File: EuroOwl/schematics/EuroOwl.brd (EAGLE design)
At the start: 100 x 99.8 mm, 121 parts, among them IC1 QUAD_OPAMPD, IC2 QUAD_OPAMPD, Q900 BC846, Q901 BC846, X1 USBPTH-VERTICAL

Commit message: Revision 01
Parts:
- R902: value 100R\ -> 100R
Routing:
- net PA2: track 64.4 -> 63.7 mm
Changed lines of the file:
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@@
 </element>
 <element name="C300" library="resistor" package="C0603" value="100n" x="71.12" y="50.8" smashed="yes">
-<attribute name="NAME" x="72.136" y="50.2285" size="1.016" layer="25" ratio="10"/>
+<attribute name="NAME" x="68.326" y="51.816" size="1.016" layer="25" ratio="10"/>
 <attribute name="VALUE" x="67.691" y="48.006" size="1.27" layer="27" ratio="10"/>
 </element>
@@
 </element>
 <element name="C500" library="resistor" package="C0603" value="100n" x="10.16" y="53.34" smashed="yes">
-<attribute name="NAME" x="9.271" y="54.102" size="1.016" layer="25"/>
+<attribute name="NAME" x="8.636" y="54.102" size="1.016" layer="25"/>
 <attribute name="VALUE" x="9.271" y="51.308" size="1.27" layer="27"/>
 </element>
@@
 <attribute name="NAME" x="73.0885" y="7.112" size="1.016" layer="25"/>
 </element>
-<element name="R902" library="Rebel" package="0603" value="100R\" x="74.93" y="11.43" smashed="yes">
+<element name="R902" library="Rebel" package="0603" value="100R" x="74.93" y="11.43" smashed="yes">
 <attribute name="NAME" x="73.0885" y="12.192" size="1.016" layer="25"/>
 </element>
@@
 </element>
 <element name="Q901" library="transistor" package="SOT23" value="BC846" x="17.78" y="21.59" smashed="yes" rot="R180">
-<attribute name="NAME" x="16.1925" y="23.1775" size="1.016" layer="25"/>
+<attribute name="NAME" x="16.1925" y="23.495" size="1.016" layer="25"/>
 <attribute name="VALUE" x="19.685" y="24.765" size="1.27" layer="27" rot="R180"/>
 </element>
 <element name="D300" library="diode" package="SOT23" value="BAT54S" x="71.12" y="54.61" smashed="yes" rot="R180">
-<attribute name="NAME" x="69.5325" y="56.1975" size="1.016" layer="25"/>
+<attribute name="NAME" x="69.5325" y="56.515" size="1.016" layer="25"/>
 <attribute name="VALUE" x="73.025" y="57.785" size="1.27" layer="27" rot="R180"/>
 </element>
 <element name="Q900" library="transistor" package="SOT23" value="BC846" x="80.01" y="7.62" smashed="yes">
-<attribute name="NAME" x="78.105" y="9.2075" size="1.016" layer="25"/>
+<attribute name="NAME" x="78.105" y="9.525" size="1.016" layer="25"/>
 <attribute name="VALUE" x="78.105" y="4.445" size="1.27" layer="27"/>
 </element>
@@
 </element>
 <element name="D500" library="diode" package="SOT23" value="BAT54S" x="6.35" y="56.1975" smashed="yes" rot="R180">
-<attribute name="NAME" x="4.7625" y="57.785" size="1.016" layer="25"/>
+<attribute name="NAME" x="4.7625" y="58.1025" size="1.016" layer="25"/>
 <attribute name="VALUE" x="8.255" y="59.3725" size="1.27" layer="27" rot="R180"/>
 </element>
 <element name="D600" library="diode" package="SOT23" value="BAT54S" x="6.35" y="35.56" smashed="yes">
-<attribute name="NAME" x="8.255" y="33.9725" size="1.016" layer="25" rot="R180"/>
+<attribute name="NAME" x="4.7625" y="37.465" size="1.016" layer="25"/>
 <attribute name="VALUE" x="4.445" y="32.385" size="1.27" layer="27"/>
 </element>
 <element name="D700" library="diode" package="SOT23" value="BAT54S" x="13.97" y="35.56" smashed="yes">
-<attribute name="NAME" x="15.875" y="33.9725" size="1.016" layer="25" font="vector" rot="R180"/>
+<attribute name="NAME" x="12.3825" y="37.465" size="1.016" layer="25" font="vector"/>
 <attribute name="VALUE" x="12.065" y="32.385" size="1.27" layer="27"/>
 </element>
 <element name="D800" library="diode" package="SOT23" value="BAT54S" x="13.97" y="55.88" smashed="yes" rot="R180">
-<attribute name="NAME" x="12.3825" y="57.4675" size="1.016" layer="25"/>
+<attribute name="NAME" x="14.605" y="57.785" size="1.016" layer="25"/>
 <attribute name="VALUE" x="15.875" y="59.055" size="1.27" layer="27" rot="R180"/>
 </element>
@@
 </element>
 <element name="C501" library="resistor" package="C0603" value="100n" x="71.12" y="40.64" smashed="yes">
-<attribute name="NAME" x="68.0085" y="38.862" size="1.016" layer="25"/>
+<attribute name="NAME" x="68.326" y="38.862" size="1.016" layer="25"/>
 <attribute name="VALUE" x="70.231" y="38.608" size="1.27" layer="27"/>
 </element>
@@
 <wire x1="54.61" y1="5.08" x2="60.325" y2="5.08" width="0.4064" layer="1"/>
 <wire x1="60.325" y1="5.08" x2="62.865" y2="7.62" width="0.4064" layer="1"/>
-<wire x1="62.865" y1="7.62" x2="66.04" y2="7.62" width="0.4064" layer="1"/>
-<via x="66.04" y="7.62" extent="1-16" drill="0.6"/>
-<wire x1="66.04" y1="7.62" x2="66.04" y2="10.16" width="0.4064" layer="16"/>
-<wire x1="66.04" y1="10.16" x2="67.31" y2="11.43" width="0.4064" layer="16"/>
+<wire x1="62.865" y1="7.62" x2="64.77" y2="7.62" width="0.4064" layer="1"/>
+<via x="64.77" y="7.62" extent="1-16" drill="0.6"/>
+<wire x1="64.77" y1="7.62" x2="64.77" y2="8.89" width="0.4064" layer="16"/>
+<wire x1="64.77" y1="8.89" x2="67.31" y2="11.43" width="0.4064" layer="16"/>
 <wire x1="67.31" y1="11.43" x2="67.31" y2="18.415" width="0.4064" layer="16"/>
 <wire x1="67.31" y1="18.415" x2="67.945" y2="19.05" width="0.4064" layer="16"/>

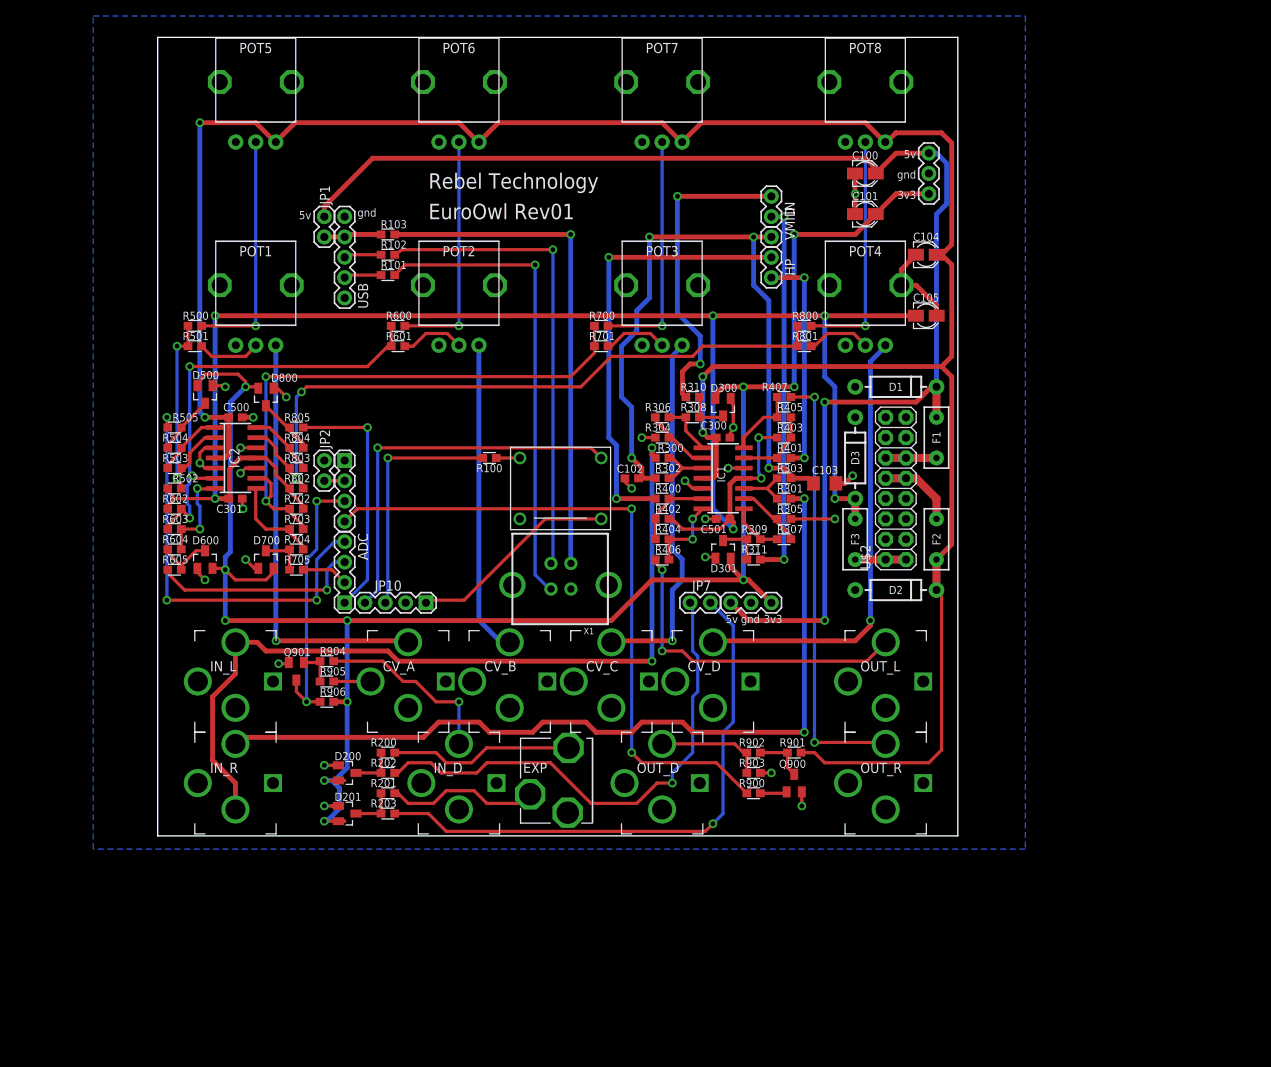
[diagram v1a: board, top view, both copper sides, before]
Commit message: changed input circuit to double inverting op amps
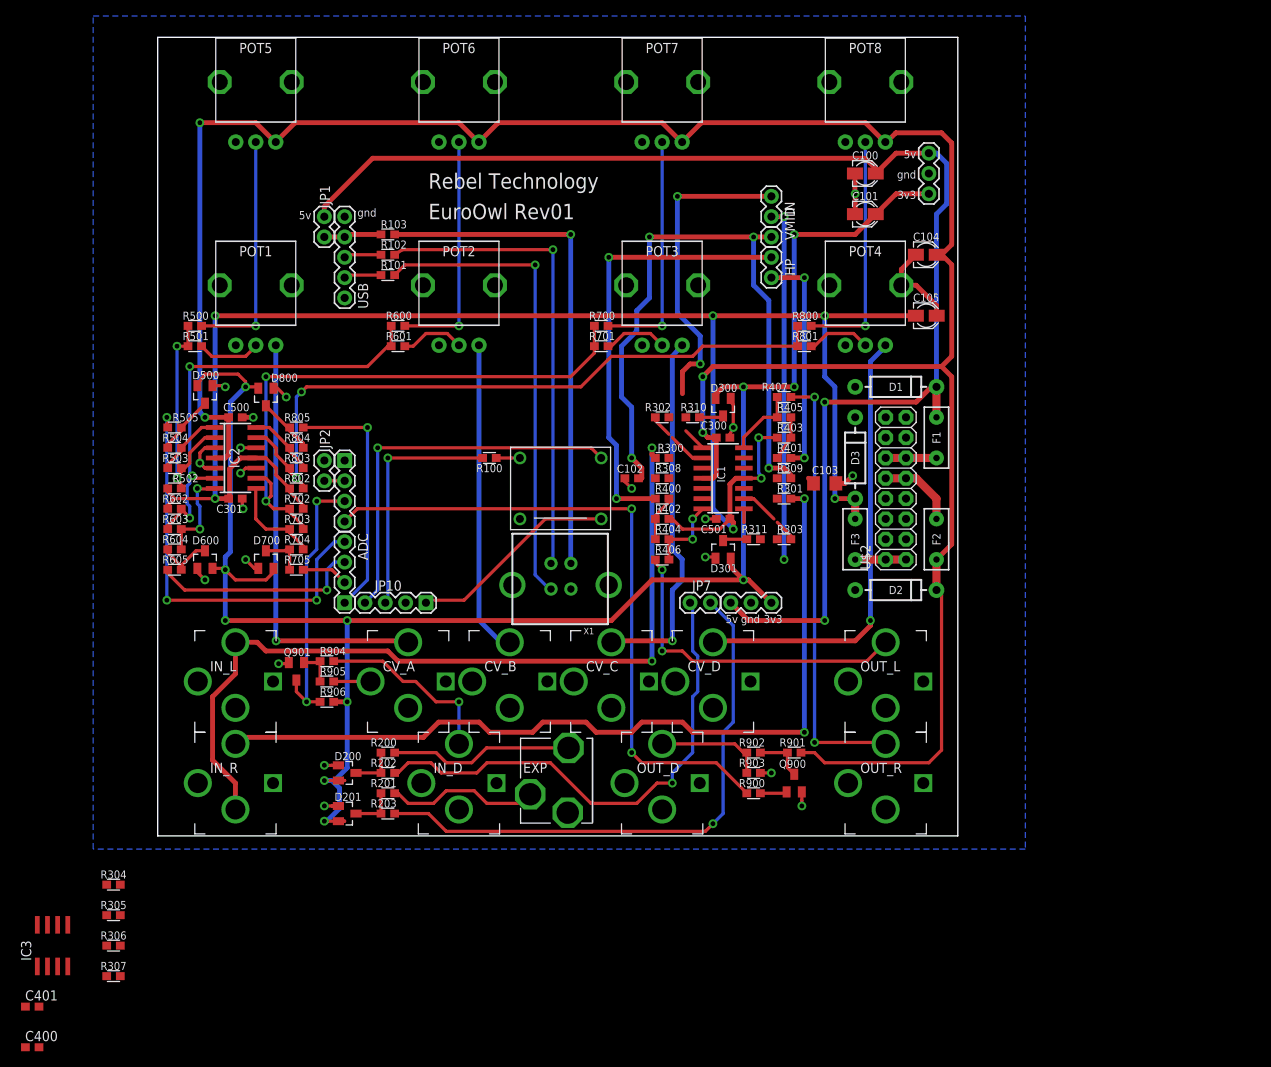
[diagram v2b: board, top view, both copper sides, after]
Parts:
- added C400, C401: 100n, resistor:C0603
- added IC3: TL072D, linear:SO08
- R302, R303: value 33k -> 100k
- R306, R307: value 33k -> 220k
- R308, R309: value 100R -> 33k
- R310, R311: value 100R -> 1k
- moved R307 100.0 mm to (-5.08, -16.5)
- moved R305 97.4 mm to (-5.08, -8.89)
- moved R306 95.2 mm to (-5.08, -12.7), turned to 0 degrees
- moved R304 88.5 mm to (-5.08, -5.08)
- moved R308 8.52 mm to (63.5, 45.7)
- moved R309 8.52 mm to (78.7, 45.7)
- moved R302 7.62 mm to (63.5, 53.3)
- moved R303 7.62 mm to (78.7, 38.1)
- moved R310 2.54 mm to (67.3, 53.3), turned to 180 degrees
- moved R311 2.54 mm to (74.9, 38.1), turned to 0 degrees
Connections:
- removed net N$11: IC1.3, R300.1, R302.1
- removed net N$8: D301.3, R309.1, R311.2
- new net N$53: IC1.14, R309.1, R311.2
- new net N$55: IC1.7, R308.1, R310.2
- new net N$57: IC1.3
- net +12V: now also C400.1, IC3.8
- net -12V: now also C401.2, IC3.4, R306.2, R307.2
- net GND: now also C400.2, C401.1, IC1.10, IC3.3, IC3.5; no longer R304.1, R305.2
- net L_IN: now also D300.3
- net N$1: now also R302.1, R304.2; no longer R306.1, R308.2
- net N$32: now also IC1.6, R304.1, R306.1, R308.2; no longer IC1.10, R301.1, R303.1
- net N$39: now also IC3.1; no longer IC1.7
- net N$4: now also R303.1, R305.2; no longer R307.1, R309.2
- net N$40: now also IC3.7; no longer IC1.14
- net N$41: now also IC3.2; no longer IC1.6
- net N$42: now also IC3.6; no longer IC1.13
- net N$5: now also R301.1, R303.2; no longer R305.1, R307.2
- net N$7: now also IC1.13, R305.1, R307.1, R309.2; no longer D300.3, R308.1, R310.2
- net N$9: now also R300.1, R302.2; no longer R304.2, R306.2
- net R_IN: now also D301.3
- net VCC/2: no longer R302.2, R303.2
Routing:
- net GND: track 73.2 -> 61.5 mm, vias 24 -> 20
- net N$11: track 6.91 -> 0.00 mm
- net N$32: track 6.49 -> 0.00 mm
- net N$7: track 5.57 -> 0.00 mm
- net N$8: track 5.57 -> 0.00 mm
- net N$4: track 6.77 -> 1.75 mm
- net VCC/2: track 86.3 -> 82.0 mm
- net N$42: track 9.77 -> 5.60 mm
- net N$41: track 9.95 -> 5.78 mm
- net N$1: track 6.77 -> 2.97 mm
- net L_IN: track 39.9 -> 42.3 mm
- net N$5: track 8.47 -> 7.63 mm
- net N$9: track 8.47 -> 7.63 mm

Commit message: rerouted input around op amp
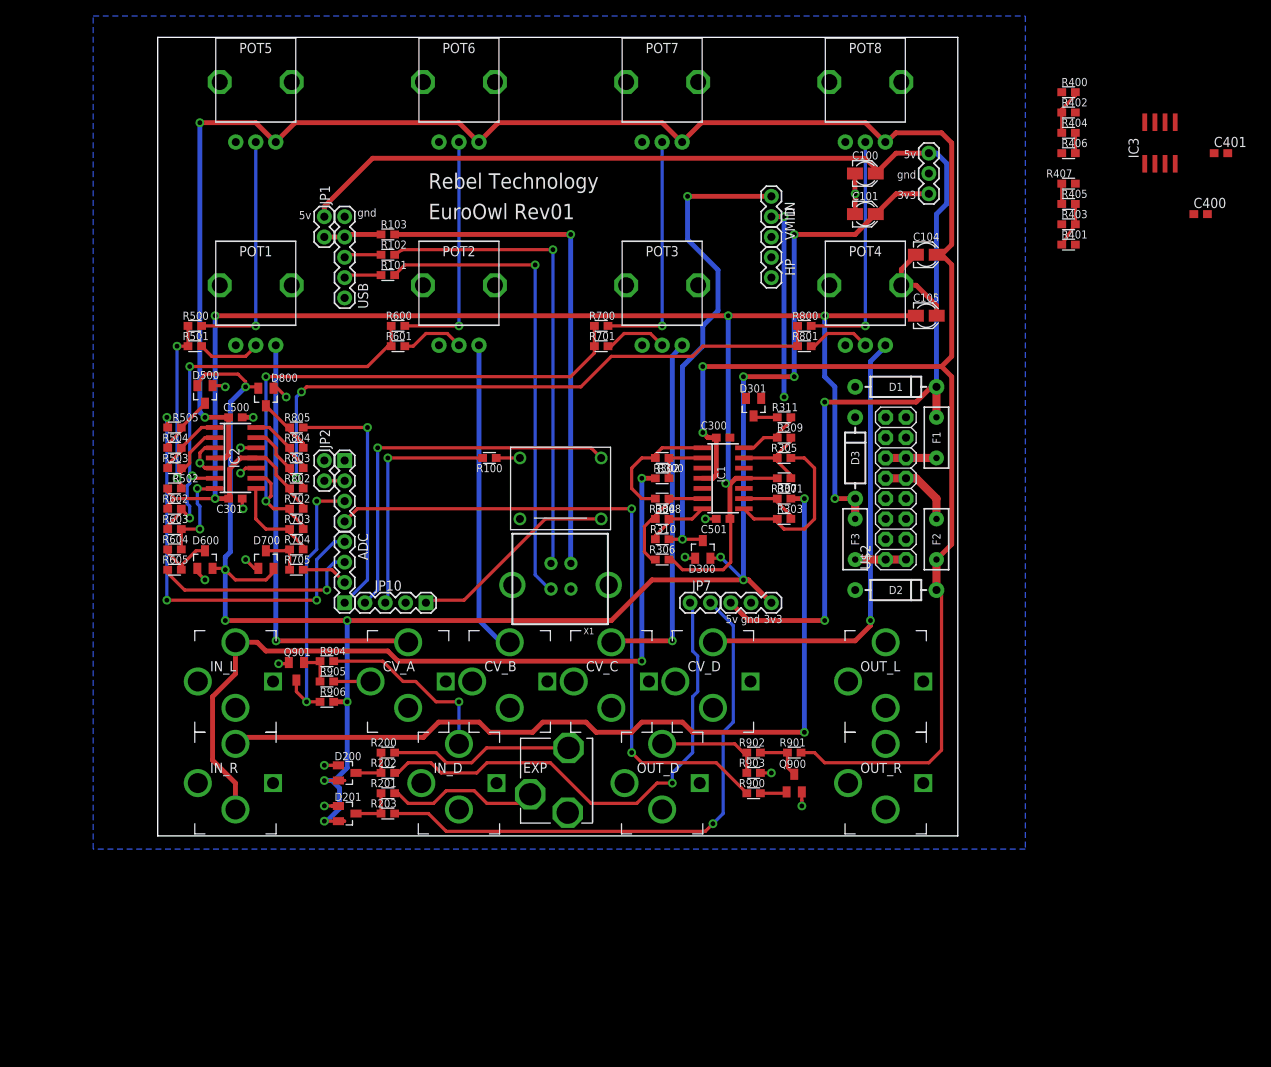
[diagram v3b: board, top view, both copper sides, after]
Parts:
- removed C102: 100n, resistor:C0603
- removed C103: 1u, resistor:C1206
- moved C401 182.9 mm to (133.3, 86.4)
- moved C400 179.4 mm to (130.8, 78.7)
- moved IC3 171.0 mm to (125.7, 87.6)
- moved R307 104.4 mm to (78.7, 45.7), turned to 180 degrees
- moved R305 101.4 mm to (78.7, 48.3)
- moved R304 83.9 mm to (63.5, 43.2), turned to 180 degrees
- moved R306 83.9 mm to (63.5, 35.6)
- moved R400 71.8 mm to (114.3, 94.0)
- moved R402 71.8 mm to (114.3, 91.4)
- moved R404 71.8 mm to (114.3, 88.9)
- moved R406 71.8 mm to (114.3, 86.4)
- moved R401 44.5 mm to (114.3, 74.9)
- moved R403 44.5 mm to (114.3, 77.5)
- moved R405 44.5 mm to (114.3, 80.0)
- moved R407 44.4 mm to (114.3, 82.5)
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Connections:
- removed net N$57: IC1.3
- net GND: now also IC1.3; no longer C102.2, C103.2
- net VCC/2: no longer C102.1, C103.1
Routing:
- net VCC/2: track 82.0 -> 0.00 mm, vias 4 -> 0
- net L_OUT: track 55.7 -> 0.00 mm, vias 2 -> 0
- net OUT_R: track 55.1 -> 0.00 mm, vias 2 -> 0
- net OUT_L: track 41.2 -> 0.00 mm, vias 2 -> 0
- net R_OUT: track 28.4 -> 0.00 mm, vias 2 -> 0
- net R_IN: track 47.5 -> 27.2 mm
- net L_IN: track 42.3 -> 61.1 mm
- net N$4: track 1.75 -> 20.5 mm
- net N$32: track 0.00 -> 14.1 mm
- net N$1: track 2.97 -> 16.2 mm
- net N$7: track 0.00 -> 10.7 mm
- net GND: track 61.5 -> 52.3 mm, vias 20 -> 17
- net -12V: track 220.0 -> 211.8 mm, vias 8 -> 6
- net N$53: track 0.00 -> 7.94 mm
- net N$55: track 0.00 -> 7.94 mm
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
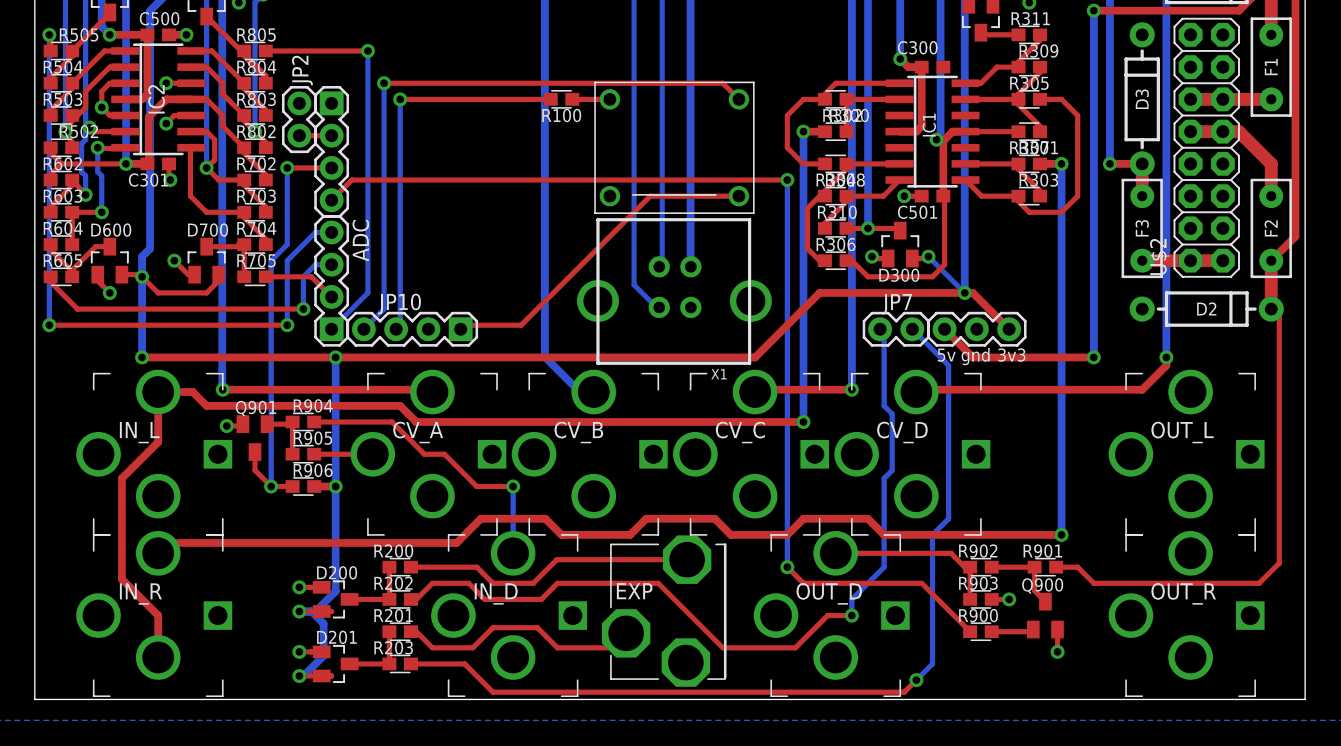
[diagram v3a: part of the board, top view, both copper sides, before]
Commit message: changed jacks to MJ355 type
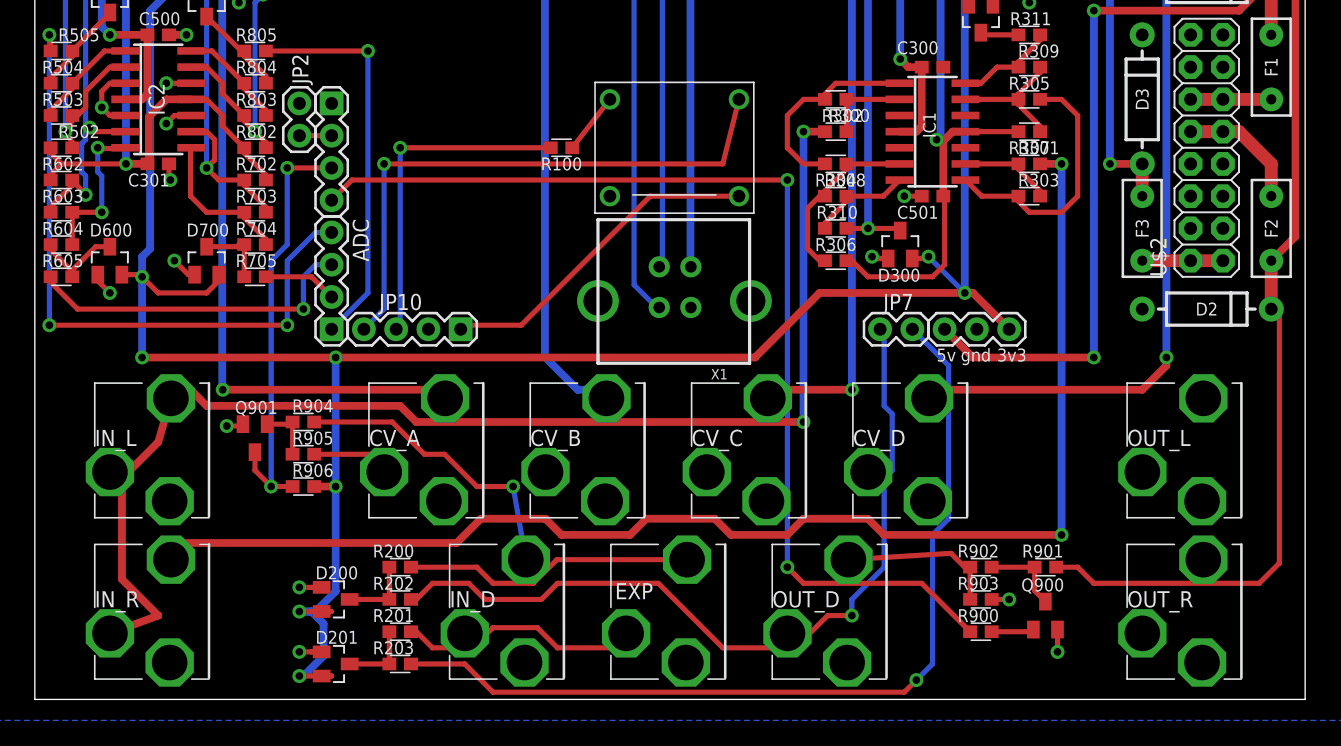
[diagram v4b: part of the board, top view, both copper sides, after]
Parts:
- CV_A, CV_B, CV_C, CV_D, IN_D, IN_L, IN_R, OUT_D, OUT_L, OUT_R: value JACK-PJ-301B -> CON-LUMBERG_1502_03; device Rebel:PJ-301B -> Rebel:CON-LUMBERG_1502_03
- moved R100 3.81 mm to (41.9, 44.5)
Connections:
- net GND: now also CV_A.P$1, CV_A.P$3, CV_B.P$1, CV_B.P$3, CV_C.P$1, CV_C.P$3, CV_D.P$1, CV_D.P$3, IN_D.P$1, IN_D.P$3, IN_L.P$1, IN_L.P$3, IN_R.P$3, OUT_D.P$3, OUT_L.P$3, OUT_R.P$3; no longer CV_A.SHL, CV_A.SLV, CV_A.SW, CV_B.SHL, CV_B.SLV, CV_B.SW, CV_C.SHL, CV_C.SLV, CV_C.SW, CV_D.SHL, CV_D.SLV, CV_D.SW, IN_D.SHL, IN_D.SLV, IN_D.SW, IN_L.SHL, IN_L.SLV, IN_R.SHL, IN_R.SLV, OUT_D.SHL, OUT_D.SLV, OUT_L.SHL, OUT_L.SLV, OUT_R.SHL, OUT_R.SLV
- net IN_L: now also IN_L.P$2, IN_R.P$1; no longer IN_L.TIP, IN_R.SW
- net IN_R: now also IN_R.P$2; no longer IN_R.TIP
- net N$18: now also CV_B.P$2; no longer CV_B.TIP
- net N$2: now also CV_A.P$2; no longer CV_A.TIP
- net N$24: now also CV_C.P$2; no longer CV_C.TIP
- net N$30: now also CV_D.P$2; no longer CV_D.TIP
- net N$46: now also IN_D.P$2; no longer IN_D.TIP
- net N$49: now also OUT_D.P$2; no longer OUT_D.TIP
- net OUT_L: now also OUT_L.P$2; no longer OUT_L.TIP
- net OUT_R: now also OUT_R.P$2; no longer OUT_R.TIP
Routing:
- net PE3: track 30.1 -> 26.3 mm
- net PE2: track 48.5 -> 45.6 mm
- net N$10: track 2.96 -> 4.82 mm
- net N$18: track 39.4 -> 40.5 mm
- net N$2: track 53.7 -> 54.7 mm
- net N$49: track 13.6 -> 12.6 mm
- net N$24: track 45.1 -> 45.9 mm
- net N$30: track 56.4 -> 57.2 mm
- net N$46: track 23.0 -> 23.6 mm
- net IN_L: track 99.6 -> 99.1 mm
